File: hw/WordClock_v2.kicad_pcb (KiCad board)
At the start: 2 copper layers, 105.5 x 33.6 mm, 25 parts, among them M1 ESP-07, P1 5V_input, P2 WS2812b_Out, P3 UART, SW1 SWITCH_INV, U1 NCP1117ST33T3G, U2 DS3232, U3 SN74LVC1T45, U4 WS2812b

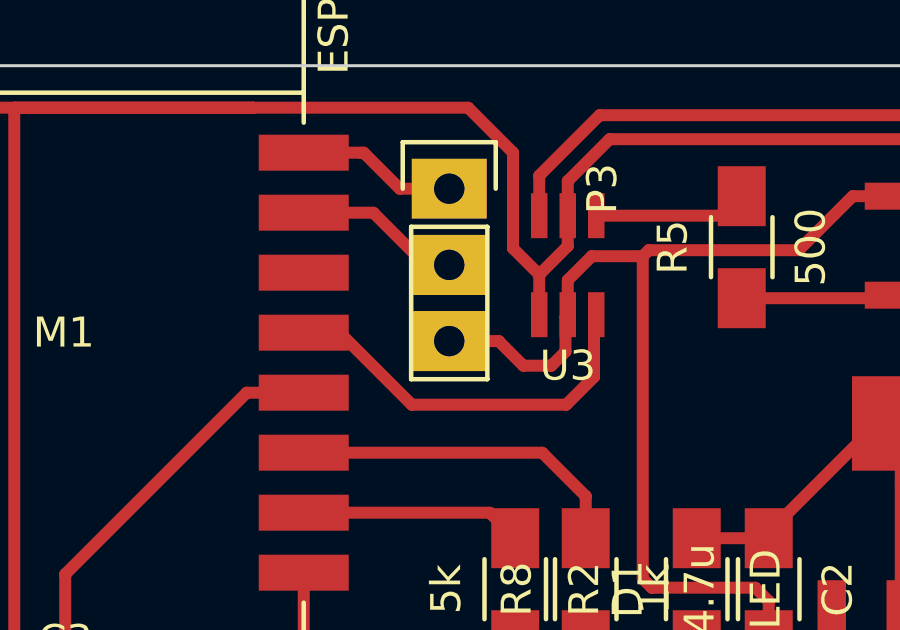
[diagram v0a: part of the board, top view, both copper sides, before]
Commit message: Updated PCB to use RDX0/GPIO3 for WS2812b in order to use the NeoEps8266Dma800KbpsMethod of Makuna's NeoPixelBus library
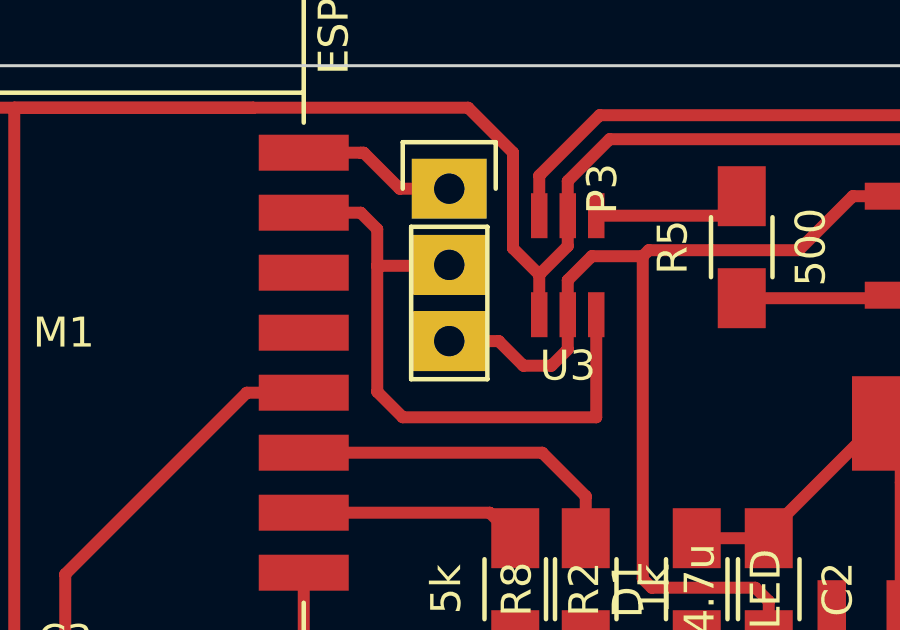
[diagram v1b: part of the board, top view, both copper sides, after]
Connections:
- M1 pad 13: WS2812b_In -> Net-(M1-Pad13)
- U3 pad 3: WS2812b_In -> UART_Rx
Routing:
- net UART_Rx: track 5.57 -> 22.5 mm
- net WS2812b_In: track 13.2 -> 0.00 mm
- net Net-(M1-Pad13): track 0.00 -> 1.20 mm

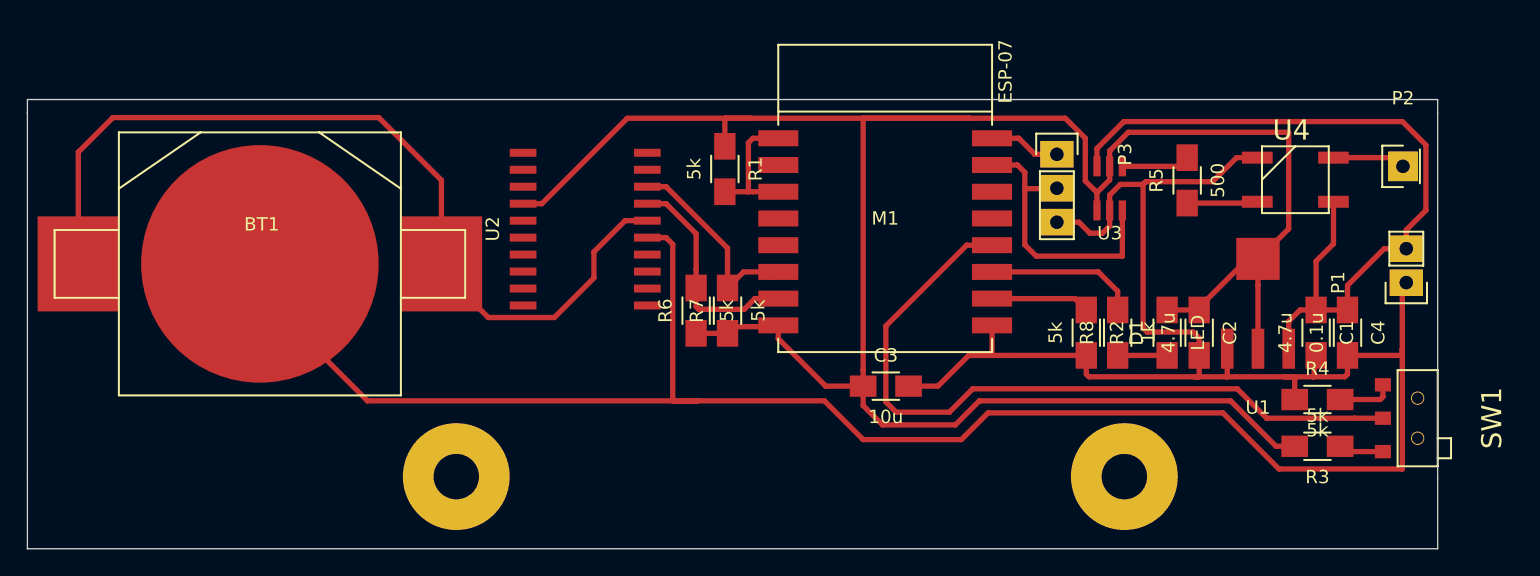
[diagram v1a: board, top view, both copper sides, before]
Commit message: Switched to diode-drop method of voltage conversion and changed from switch to push button for entering programming mode
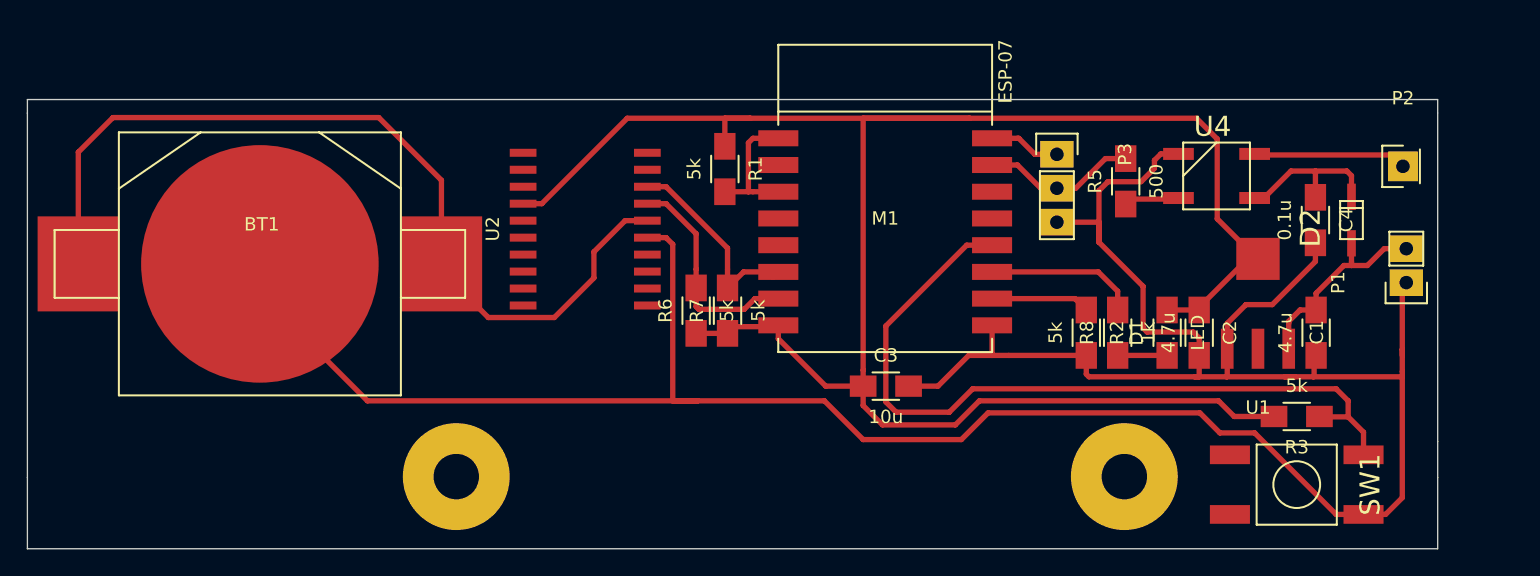
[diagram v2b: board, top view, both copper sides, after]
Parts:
- removed R4: 5k, FabLibrary:C_1206_HandSoldering_IainEdit
- removed U3: SN74LVC1T45, FabLibrary:TI-DBV-SOT23_handsolder
- added D2: D, IainPersonalLibrary:SOD-123F_HandSolder, F.Cu at (159.1, 70.2)
- SW1: value SWITCH_INV -> DPST; footprint FabLibrary:SlideSwitch_smd -> IainPersonalLibrary:FSM2JSMA_DPST_PushButton
- moved SW1 10.3 mm to (154.9, 90.0)
- moved C4 8.76 mm to (156.3, 70.2)
- moved U4 5.91 mm to (148.9, 66.9)
- moved R5 4.60 mm to (142.2, 67.3)
- moved R3 2.72 mm to (154.9, 84.9)
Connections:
- C4 pad 1: +5VD -> Net-(C4-Pad1)
- R3 pad 1: Net-(R3-Pad1) -> GPIO0
- R5 pad 2: Net-(R5-Pad2) -> UART_Rx
- SW1 pad 1: Net-(R3-Pad1) -> Net-(SW1-Pad1)
- U4 pad 1: +5VD -> Net-(C4-Pad1)
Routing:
- net +5VD: track 58.8 -> 15.8 mm
- net +3V3: track 180.0 -> 157.1 mm
- net Net-(C4-Pad1): track 0.00 -> 11.8 mm
- net UART_Rx: track 22.5 -> 12.4 mm
- net Net-(P2-Pad1): track 5.47 -> 12.4 mm
- net GND: track 215.1 -> 221.6 mm
- net Net-(R5-Pad2): track 5.59 -> 0.00 mm
- net Net-(SW1-Pad3): track 4.38 -> 0.00 mm
- net Net-(R3-Pad1): track 3.93 -> 0.00 mm
- net GPIO0: track 55.3 -> 58.8 mm
- net Net-(R5-Pad1): track 5.29 -> 4.14 mm
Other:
- board text added: "3.3V internal connection on regulator"

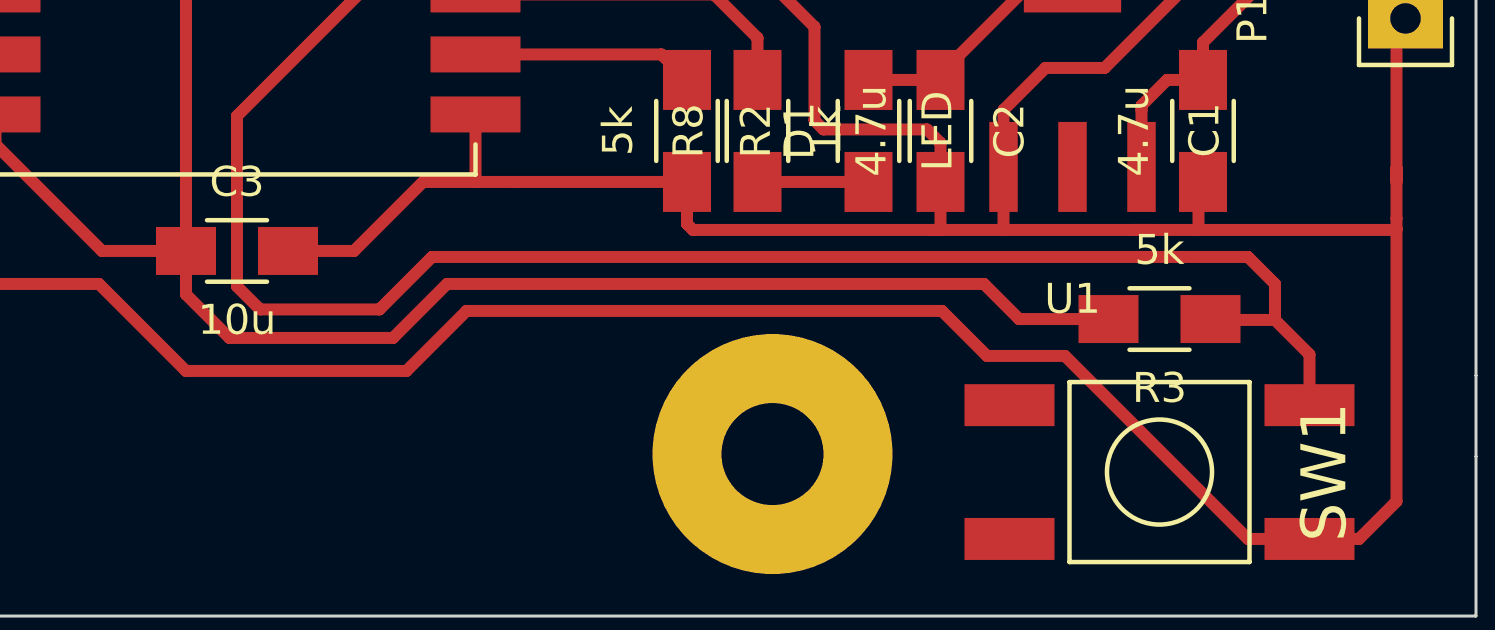
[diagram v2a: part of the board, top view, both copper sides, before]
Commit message: fixed clearnace issue for making on the denford
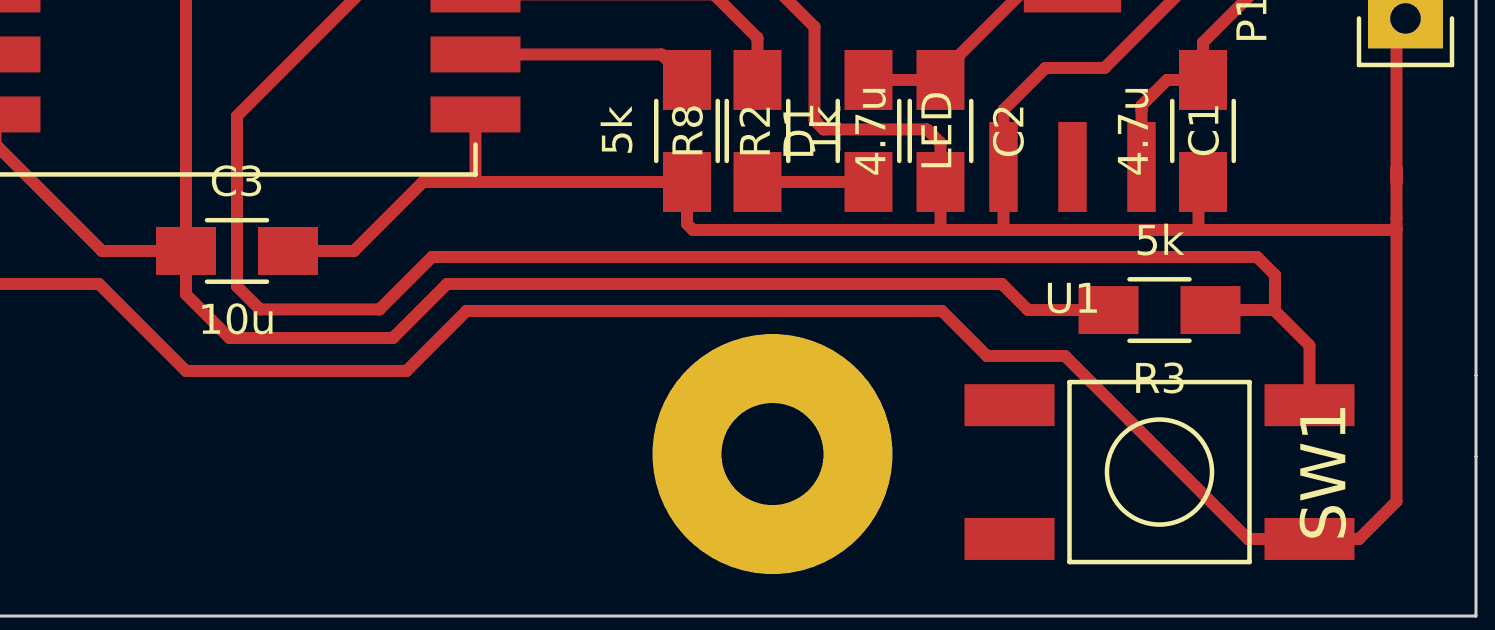
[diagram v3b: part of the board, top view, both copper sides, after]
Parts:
- moved R3 0.30 mm to (154.9, 84.6)
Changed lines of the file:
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@@
     (links 45)
     (no_connects 1)
-    (area 59.899999 61.099999 165.550001 94.820001)
+    (area 59.899999 55.575 197.05 96.09998)
     (thickness 1.6)
     (drawings 11)
-    (tracks 211)
+    (tracks 213)
     (zones 0)
     (modules 24)
@@
   )
   (module FabLibrary:C_1206_HandSoldering_IainEdit (layer F.Cu)
-    (at 154.95 84.87 180)
+    (at 154.95 84.57 180)
     (descr "Capacitor SMD 1206, hand soldering")
     (tags "capacitor 1206")
@@
   (segment (start 156.4 76.9) (end 155.2 76.9) (width 0.4) (layer F.Cu) (net 3))
   (segment (start 163.15 72.2) (end 163.15 72.31) (width 0.4) (layer F.Cu) (net 3))
+  (segment (start 122.5 82.6) (end 122.5 84.05) (width 0.4) (layer F.Cu) (net 4))
+  (segment (start 122.5 84.05) (end 123.95 85.5) (width 0.4) (layer F.Cu) (net 4))
+  (segment (start 123.95 85.5) (end 129.4 85.5) (width 0.4) (layer F.Cu) (net 4))
+  (segment (start 129.4 85.5) (end 131.2 83.7) (width 0.4) (layer F.Cu) (net 4))
+  (segment (start 131.2 83.7) (end 149.7 83.7) (width 0.4) (layer F.Cu) (net 4))
+  (segment (start 150.57 84.57) (end 153.25 84.57) (width 0.4) (layer F.Cu) (net 4))
+  (segment (start 149.7 83.7) (end 150.57 84.57) (width 0.4) (layer F.Cu) (net 4))
   (segment (start 130.469998 62.55) (end 147.45 62.55) (width 0.4) (layer F.Cu) (net 4))
   (segment (start 147.45 62.55) (end 149 64.1) (width 0.4) (layer F.Cu) (net 4))
@@
   (segment (start 149 70.075) (end 152 73.075) (width 0.4) (layer F.Cu) (net 4))
   (segment (start 152 73.075) (end 152.05 73.075) (width 0.4) (layer F.Cu) (net 4))
-  (segment (start 153.25 84.87) (end 150.27 84.87) (width 0.4) (layer F.Cu) (net 4))
-  (segment (start 150.27 84.87) (end 149.1 83.7) (width 0.4) (layer F.Cu) (net 4))
-  (segment (start 149.1 83.7) (end 131.2 83.7) (width 0.4) (layer F.Cu) (net 4))
-  (segment (start 131.2 83.7) (end 129.4 85.5) (width 0.4) (layer F.Cu) (net 4))
-  (segment (start 129.4 85.5) (end 123.95 85.5) (width 0.4) (layer F.Cu) (net 4))
-  (segment (start 123.95 85.5) (end 122.5 84.05) (width 0.4) (layer F.Cu) (net 4))
-  (segment (start 122.5 84.05) (end 122.5 82.6) (width 0.4) (layer F.Cu) (net 4))
   (segment (start 145.25 76.9) (end 147.65 76.9) (width 0.4) (layer F.Cu) (net 4))
   (segment (start 152.1 73.075) (end 152.05 73.075) (width 0.4) (layer F.Cu) (net 4))
@@
   (segment (start 130.25 72.05) (end 124.2 78.1) (width 0.4) (layer F.Cu) (net 11))
   (segment (start 124.2 78.1) (end 124.2 83.780002) (width 0.4) (layer F.Cu) (net 11))
-  (segment (start 158.8 83.7) (end 158.8 84.9) (width 0.4) (layer F.Cu) (net 11))
   (segment (start 124.2 83.780002) (end 124.969998 84.55) (width 0.4) (layer F.Cu) (net 11))
-  (segment (start 130.7 82.8) (end 157.9 82.8) (width 0.4) (layer F.Cu) (net 11))
   (segment (start 124.969998 84.55) (end 128.95 84.55) (width 0.4) (layer F.Cu) (net 11))
   (segment (start 128.95 84.55) (end 130.7 82.8) (width 0.4) (layer F.Cu) (net 11))
-  (segment (start 157.9 82.8) (end 158.8 83.7) (width 0.4) (layer F.Cu) (net 11))
+  (segment (start 158.8 83.4) (end 158.8 84.57) (width 0.4) (layer F.Cu) (net 11))
+  (segment (start 130.7 82.8) (end 158.2 82.8) (width 0.4) (layer F.Cu) (net 11))
+  (segment (start 158.2 82.8) (end 158.8 83.4) (width 0.4) (layer F.Cu) (net 11))
+  (segment (start 158.8 84.57) (end 158.8 84.6) (width 0.4) (layer F.Cu) (net 11))
+  (segment (start 158.8 84.6) (end 159.95 85.75) (width 0.4) (layer F.Cu) (net 11))
+  (segment (start 159.95 85.75) (end 159.95 87.74) (width 0.4) (layer F.Cu) (net 11))
+  (segment (start 156.65 84.57) (end 158.05 84.57) (width 0.4) (layer F.Cu) (net 11))
+  (segment (start 158.05 84.57) (end 158.8 84.57) (width 0.4) (layer F.Cu) (net 11))
   (segment (start 156.65 84.87) (end 156.85 84.87) (width 0.4) (layer F.Cu) (net 11))
   (segment (start 156.85 84.87) (end 156.88 84.9) (width 0.4) (layer F.Cu) (net 11))
-  (segment (start 156.88 84.9) (end 158.8 84.9) (width 0.4) (layer F.Cu) (net 11))
-  (segment (start 158.8 84.9) (end 159.95 86.05) (width 0.4) (layer F.Cu) (net 11))
-  (segment (start 159.95 86.05) (end 159.95 87.74) (width 0.4) (layer F.Cu) (net 11))
   (segment (start 137 67.79) (end 138.41 67.79) (width 0.4) (layer F.Cu) (net 13))
   (segment (start 138.41 67.79) (end 140.63 65.57) (width 0.4) (layer F.Cu) (net 13))

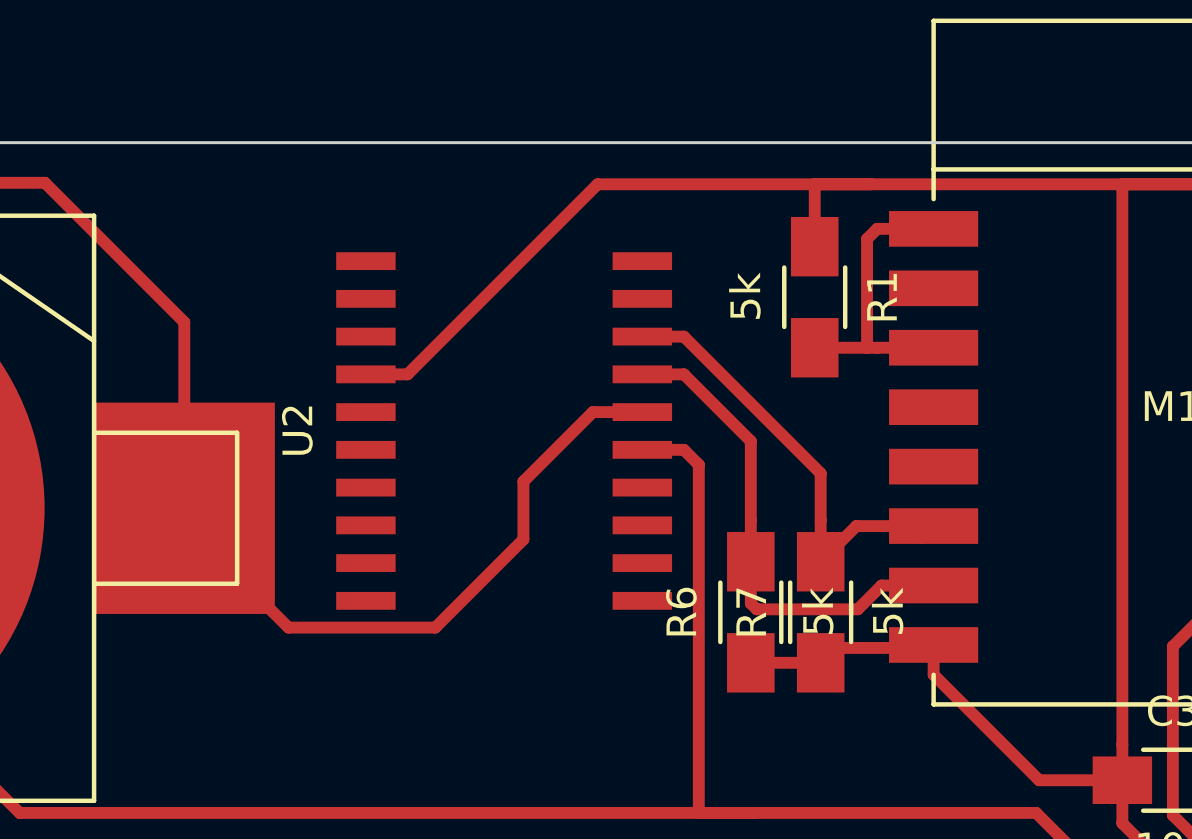
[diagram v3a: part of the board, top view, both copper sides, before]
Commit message: Updated CH_PD and RST on ESP to use their own pullup resistors. Attached GPIO16 to RST to allow wake from deep sleep
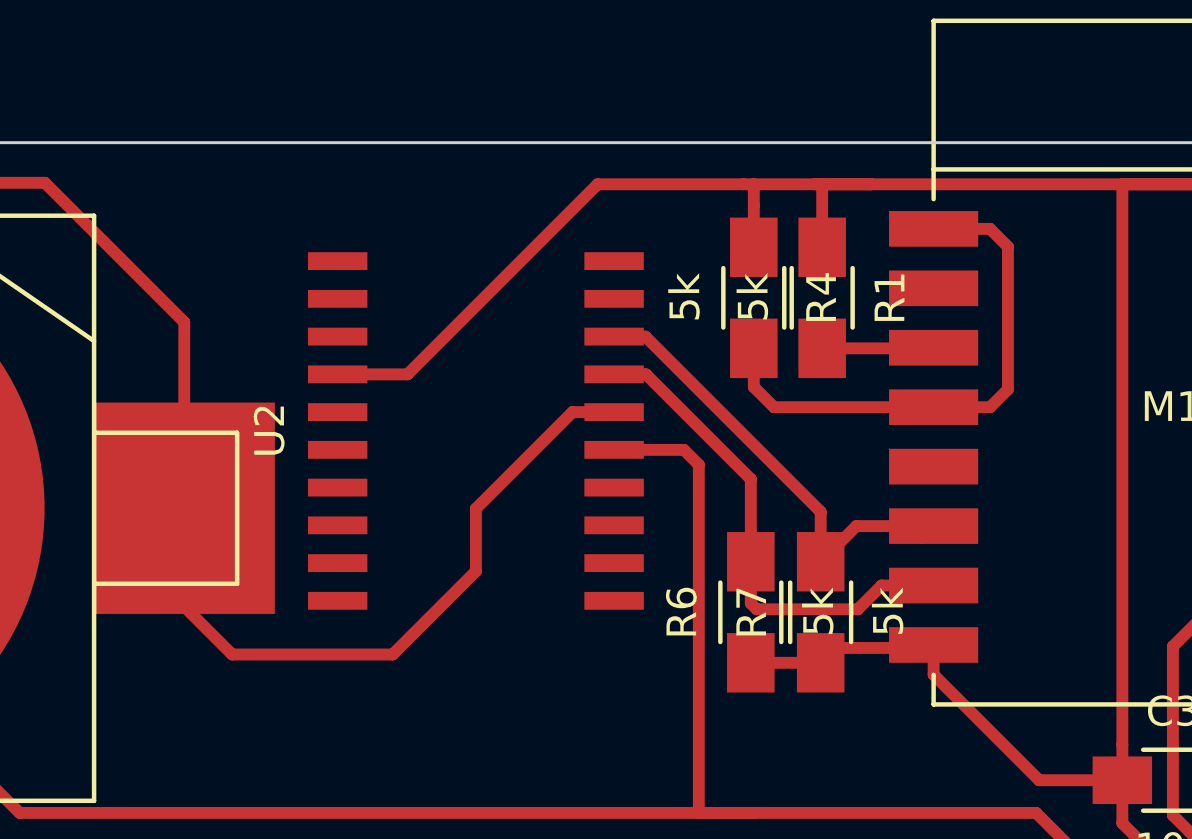
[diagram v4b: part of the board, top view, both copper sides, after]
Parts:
- added R4: 5k, FabLibrary:C_1206_HandSoldering_IainEdit, F.Cu at (110.1, 66.4)
- moved U2 0.95 mm to (100.8, 70.8)
- moved R1 0.25 mm to (112.4, 66.4)
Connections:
- M1 pad 3: Net-(M1-Pad1) -> Net-(M1-Pad3)
- M1 pad 4: Net-(M1-Pad4) -> Net-(M1-Pad1)
- R1 pad 2: Net-(M1-Pad1) -> Net-(M1-Pad3)
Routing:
- net Net-(M1-Pad1): track 10.0 -> 17.9 mm
- net Net-(M1-Pad3): track 0.00 -> 3.76 mm
- net +3V3: track 157.0 -> 160.1 mm
- net Net-(BT1-Pad1): track 66.3 -> 67.9 mm
- net GND: track 221.6 -> 222.6 mm
